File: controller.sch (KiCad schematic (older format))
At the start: 50 parts, among them CON1 SD_Card, IC1 ATMEGA328-A, P1 ISP, P10 RS485, P2 BUTTONS, P3 OPEN_DRAIN, P4 POWER, P5 I2C1, P6 I2C2, P8 THERMOCOUPLE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

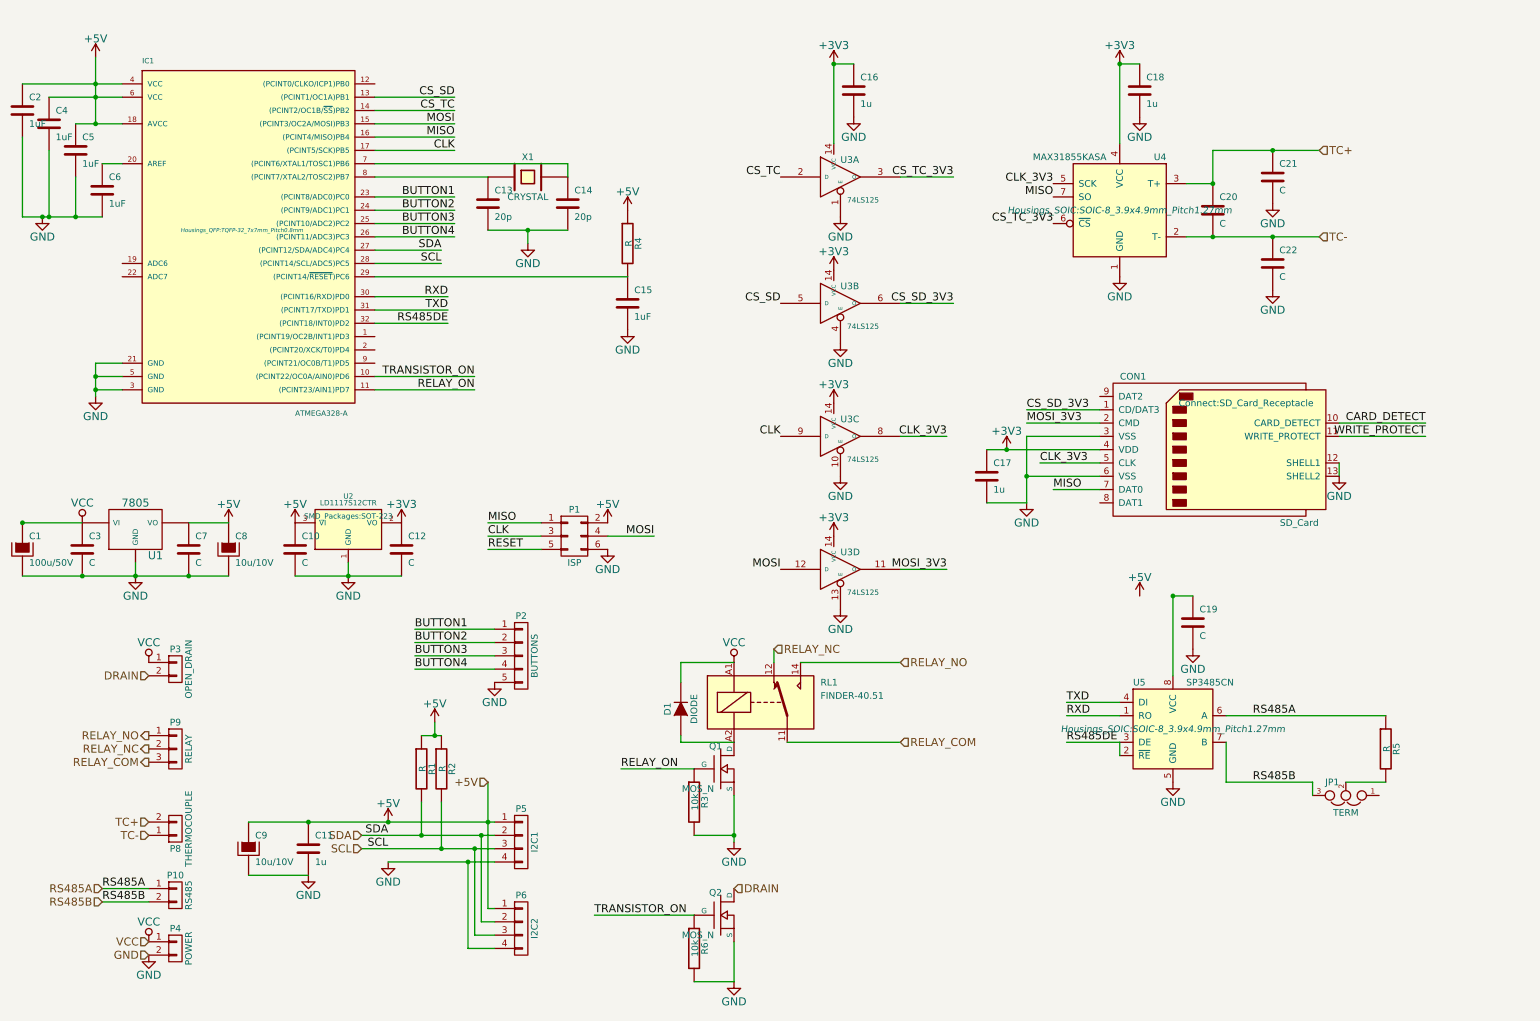
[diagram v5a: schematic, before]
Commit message: Add the correct relay footprint, solve MISO voltage level conversion, route the PCB
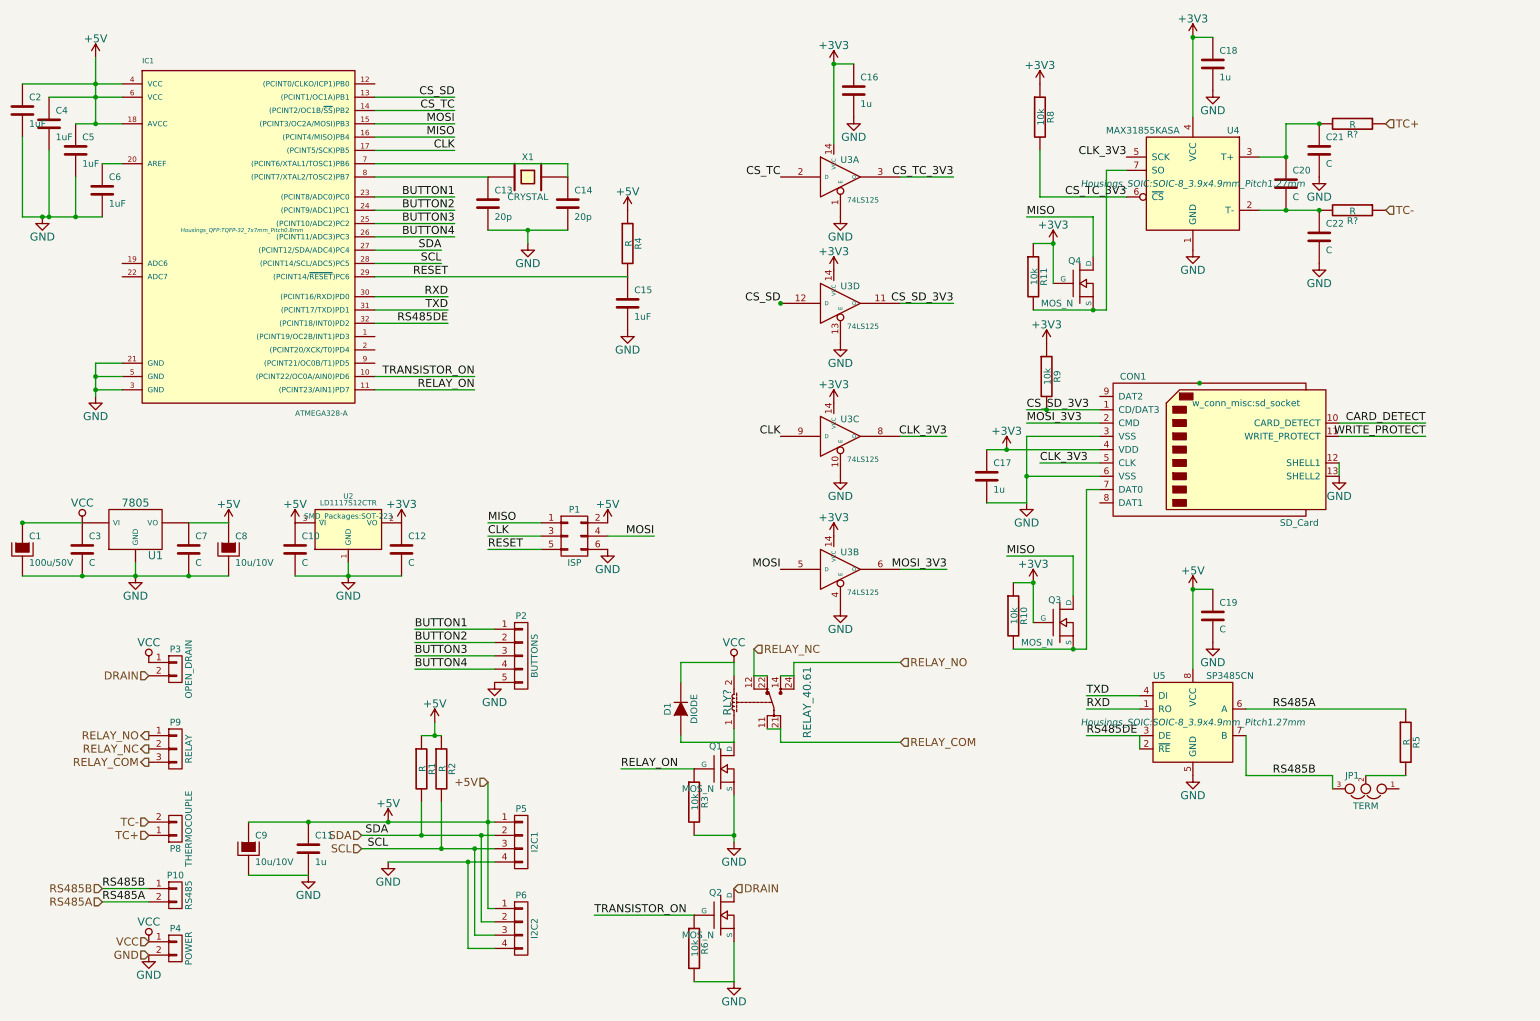
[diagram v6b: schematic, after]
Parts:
- removed RL1: FINDER-40.51, Relays_ThroughHole:Relay_DPDT_Schrack-RT2_RM5mm, symbol FINDER-40.51
- added Q3, Q4: MOS_N, Transistors_SMD:sot23, symbol MOS_N
- added R10, R11, R8, R9: 10k, Resistors_SMD:R_0603_HandSoldering, symbol R
- added R? (x2): R, symbol R
- added RLY?: RELAY_40.61, symbol RELAY_40.61
- CON1: footprint Connect:SD_Card_Receptacle -> w_conn_misc:sd_socket
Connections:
- net +3V3: now also Q3.G, Q4.G, R10.1, R11.1, R8.1, R9.1
- net +5V: now also C19.1, U5.8 (VCC)
- net CS_SD: now also U3.12 (D); no longer U3.5 (D)
- net CS_SD_3V3: now also U3.11 (O), R9.2; no longer U3.6 (O)
- net CS_TC_3V3: now also R8.2
- net MISO: now also Q3.D, Q4.D; no longer CON1.7 (DAT0), U4.7 (SO)
- net MOSI: now also U3.5 (D); no longer U3.12 (D)
- net MOSI_3V3: now also U3.6 (O); no longer U3.11 (O)
- net RELAY_COM: now also RLY?.11, RLY?.21
- net RELAY_NC: now also RLY?.12, RLY?.22
- net RELAY_NO: now also RLY?.14, RLY?.24
- net RESET: now also C15.1, IC1.29 ((PCINT14/~RESET~)PC6), R4.2
- net RS485A: now also P10.2 (P2); no longer P10.1 (P1)
- net RS485B: now also P10.1 (P1); no longer P10.2 (P2)
- net TC+: now also P8.1 (P1), R?.1; no longer C20.1, C21.1, P8.2 (P2), U4.3 (T+)
- net TC-: now also P8.2 (P2), R?.1; no longer C20.2, C22.1, P8.1 (P1), U4.2 (T-)
- net VCC: now also RLY?.2
- net at D1.1 (A), Q1.D: now also RLY?.1
- new net: C20.2, C22.1, R?.2, U4.2 (T-)
- new net: C20.1, C21.1, R?.2, U4.3 (T+)
- new net: Q4.S, R11.2, U4.7 (SO)
- new net: CON1.7 (DAT0), Q3.S, R10.2
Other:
- moved on the sheet: C18, C19, C20, C21, C22, JP1, R5, U3B, U3D, U4, U5

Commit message: Shorten the board, reroute
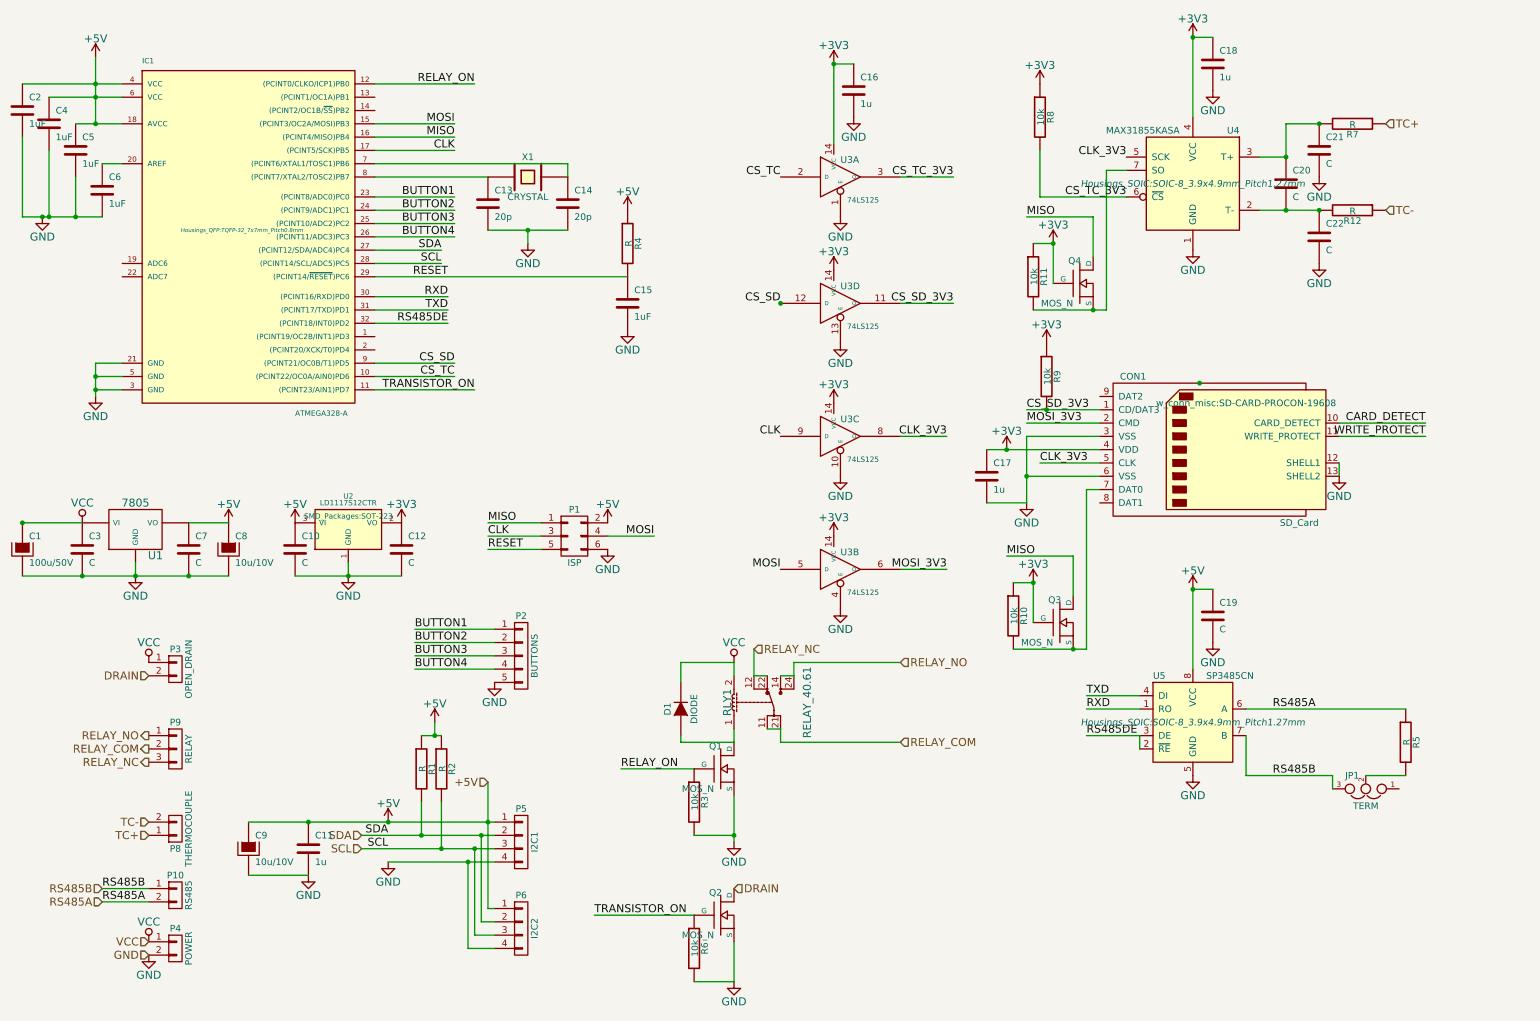
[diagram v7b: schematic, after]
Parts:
- CON1: footprint w_conn_misc:sd_socket -> w_conn_misc:SD-CARD-PROCON-19608
- gave numbers to parts that had none: 3
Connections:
- net CS_SD: now also IC1.9 ((PCINT21/OC0B/T1)PD5); no longer IC1.13 ((PCINT1/OC1A)PB1)
- net CS_TC: now also IC1.10 ((PCINT22/OC0A/AIN0)PD6); no longer IC1.14 ((PCINT2/OC1B/~SS~)PB2)
- net RELAY_COM: now also P9.2 (P2); no longer P9.3 (P3)
- net RELAY_NC: now also P9.3 (P3); no longer P9.2 (P2)
- net RELAY_ON: now also IC1.12 ((PCINT0/CLKO/ICP1)PB0); no longer IC1.11 ((PCINT23/AIN1)PD7)
- net TRANSISTOR_ON: now also IC1.11 ((PCINT23/AIN1)PD7); no longer IC1.10 ((PCINT22/OC0A/AIN0)PD6)

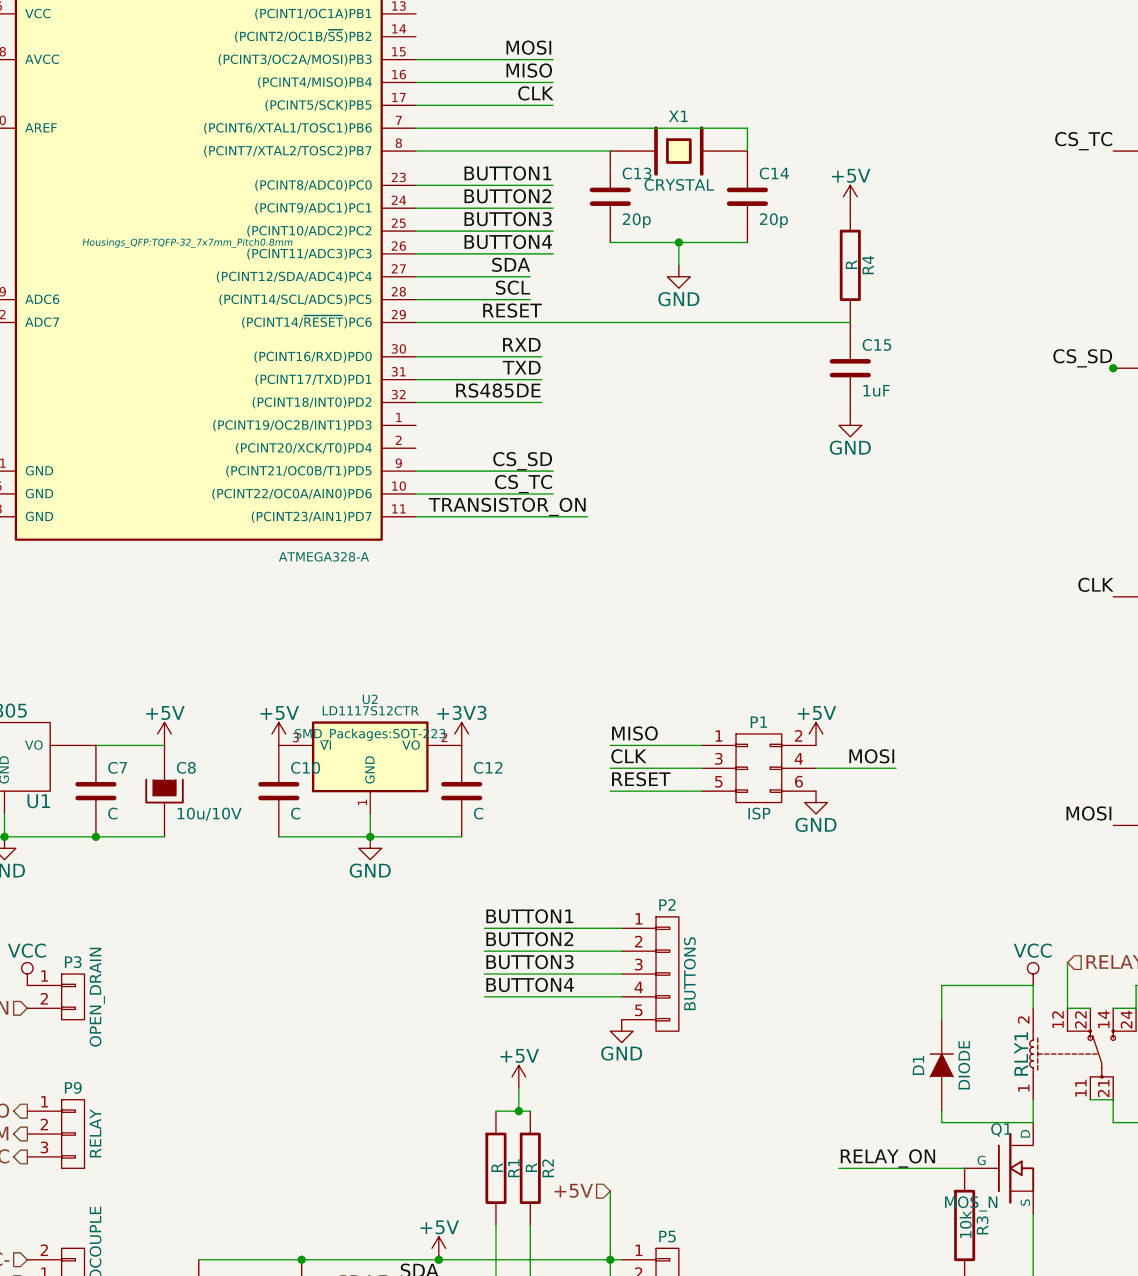
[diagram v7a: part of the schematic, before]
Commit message: Add a serial header for Arduino compatible programming
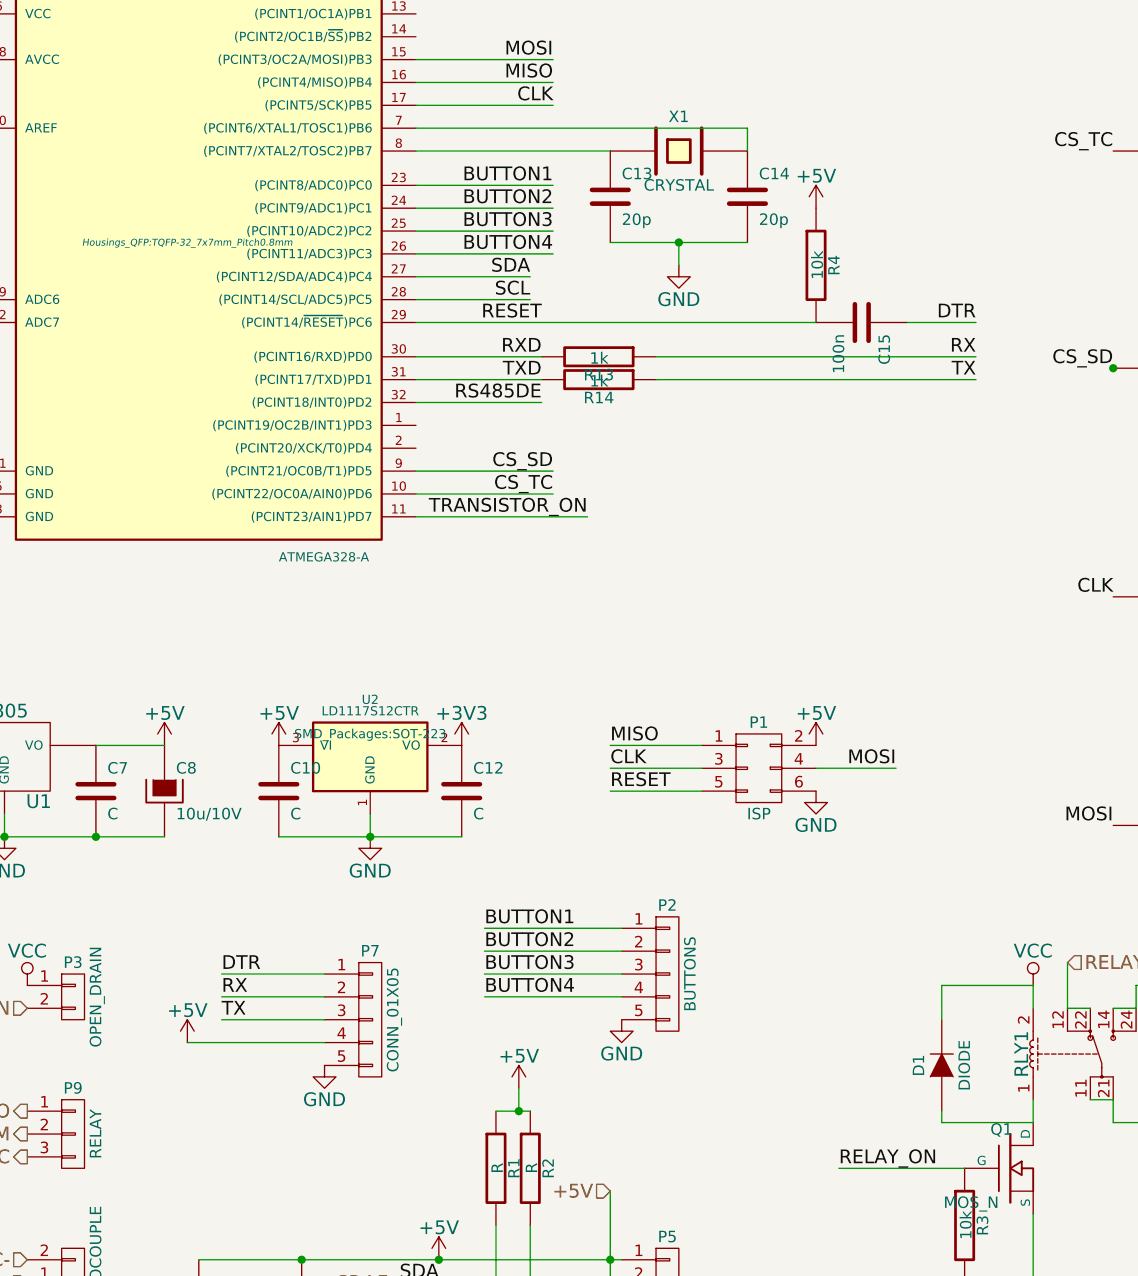
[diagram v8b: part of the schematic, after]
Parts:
- added P7: CONN_01X05, symbol CONN_01X05
- added R13, R14: 1k, Resistors_SMD:R_0603_HandSoldering, symbol R
- C15: value 1uF -> 100n; footprint Capacitors_SMD:C_0603_HandSoldering -> (none)
- R4: value R -> 10k
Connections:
- net +5V: now also P7.4 (P4)
- net GND: now also P7.5 (P5); no longer C15.2
- net RESET: now also C15.2; no longer C15.1
- net RXD: now also R13.2
- net TXD: now also R14.2
- new net DTR: C15.1, P7.1 (P1)
- new net RX: P7.2 (P2), R13.1
- new net TX: P7.3 (P3), R14.1
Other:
- moved on the sheet: R4
